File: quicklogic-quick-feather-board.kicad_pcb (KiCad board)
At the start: 2 copper layers, 50.8 x 22.9 mm, 4 parts, among them IC1 EOS-S3, J5 0473460001

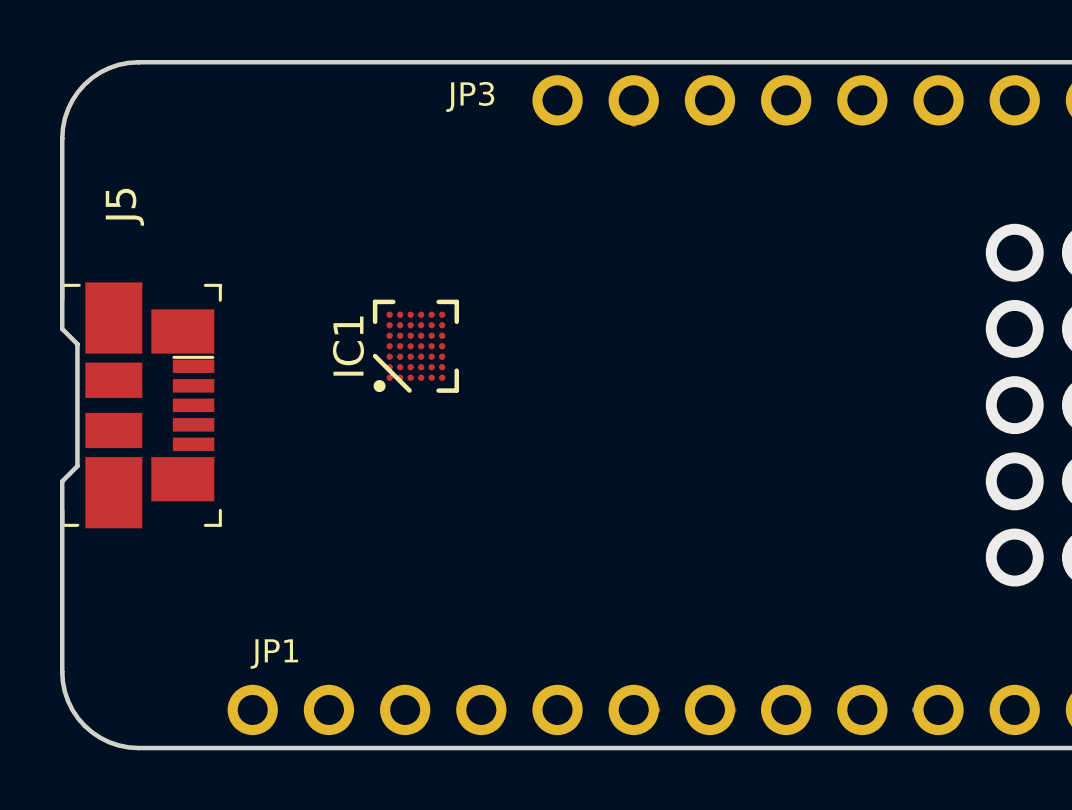
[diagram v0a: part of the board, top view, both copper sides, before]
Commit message: Added power supply circuits
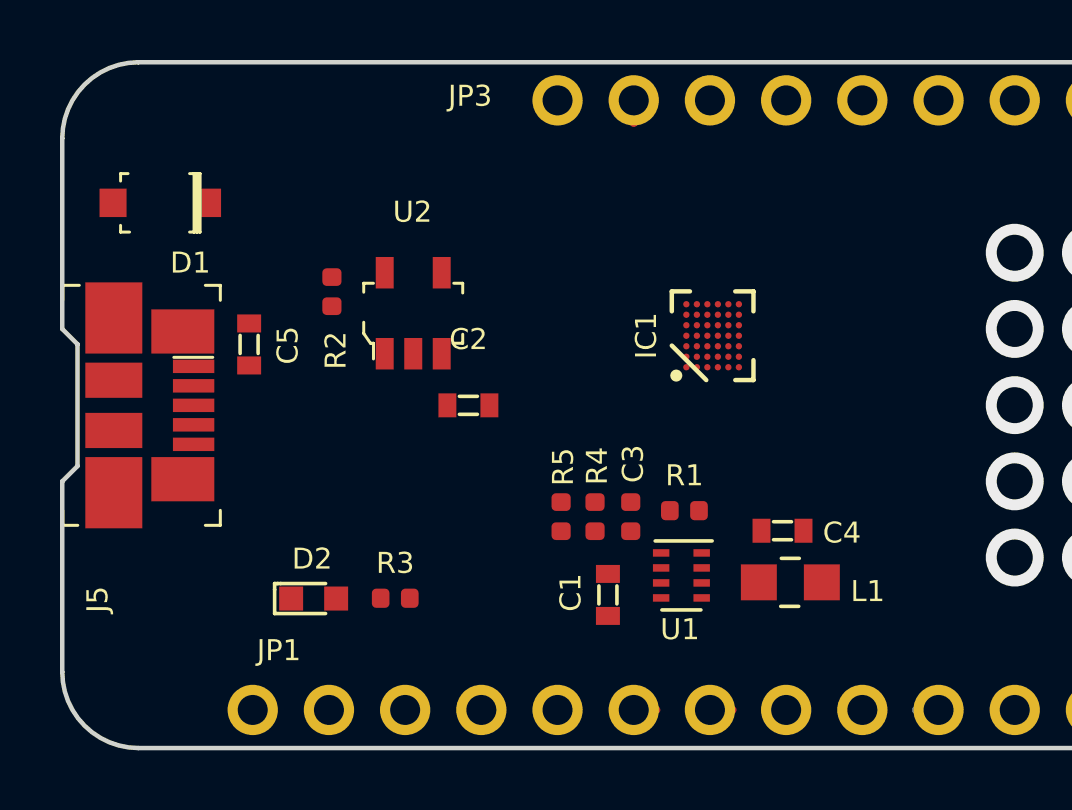
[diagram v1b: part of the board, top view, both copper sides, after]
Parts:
- added C1: C_4u7_0603, antmicro-footprints:0603-cap, F.Cu at (141.3, 111.3)
- added C2: C_10u_0603, antmicro-footprints:0603-cap, F.Cu at (136.6, 105.0)
- added C3: C_100p_0402, antmicro-footprints:0402-cap, F.Cu at (142.1, 108.7)
- added C4: C_22u_0603, antmicro-footprints:0603-cap, F.Cu at (147.1, 109.2)
- added C5: C_10u_0603, antmicro-footprints:0603-cap, F.Cu at (129.3, 103.0)
- added D1: MBR0520LT1G, antmicro-footprints:SOD-123, F.Cu at (126.4, 98.3)
- added D2: LG_L29K-G2J1-24-Z, antmicro-footprints:LED_0603, F.Cu at (131.5, 111.5)
- added L1: DFE201610E-R47M=P2, antmicro-footprints:0805-res, F.Cu at (147.4, 110.9)
- added R1: R_100k_0402, antmicro-footprints:0402-res, F.Cu at (143.8, 108.5)
- added R2: R_5k11_0402, antmicro-footprints:0402-res, F.Cu at (132.1, 101.2)
- added R3: R_1k_0402, antmicro-footprints:0402-res, F.Cu at (134.2, 111.4)
- added R4: R_100k_0402, antmicro-footprints:0402-res, F.Cu at (140.9, 108.7)
- added R5: R_100k_0402, antmicro-footprints:0402-res, F.Cu at (139.7, 108.7)
- added U1: TPS62821DLCR, antmicro-footprints:QFN-8_2x1mm, F.Cu at (143.7, 110.7)
- added U2: MCP73831T-2ACI_OT, antmicro-footprints:SOT-753, F.Cu at (134.8, 101.9)
- moved IC1 9.90 mm to (144.8, 102.7)
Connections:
- J5 pad 1: /5V0_USB -> /VBUS

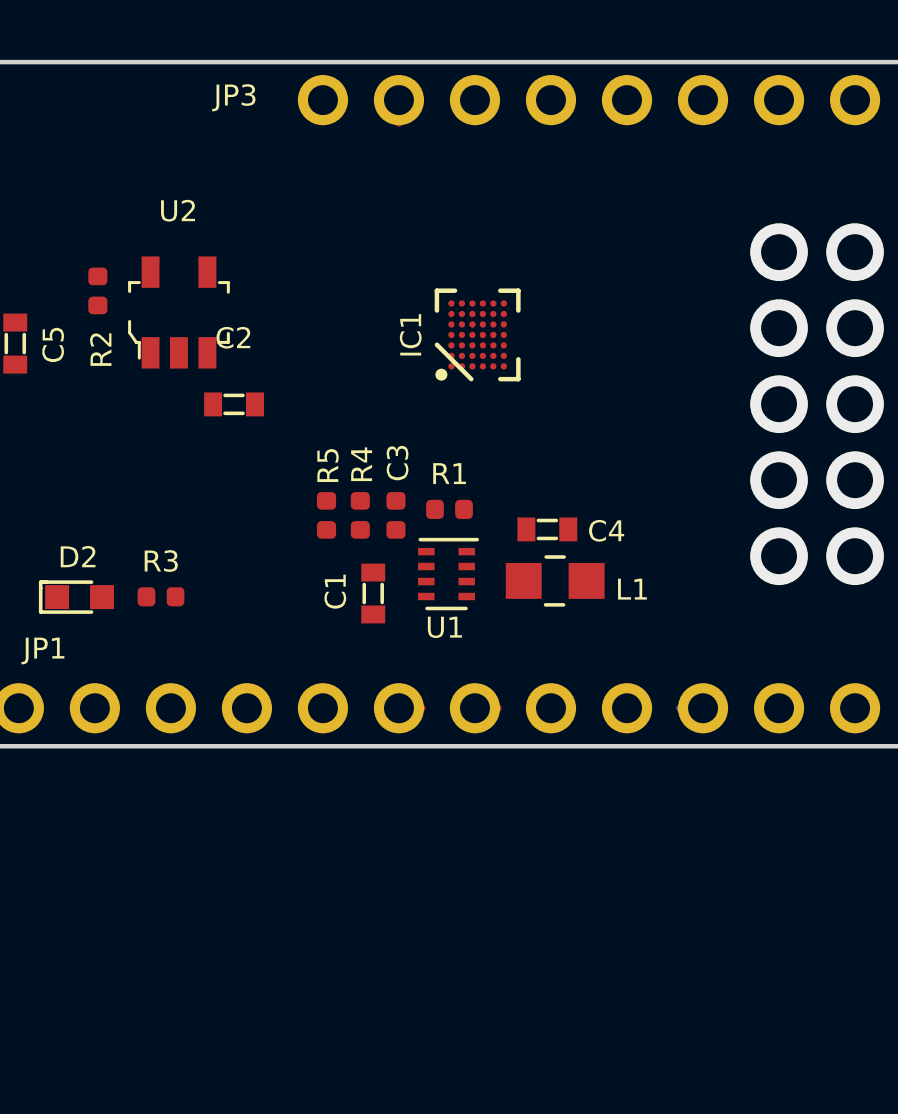
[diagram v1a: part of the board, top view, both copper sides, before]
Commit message: Added flash memory and 32kHz crystal
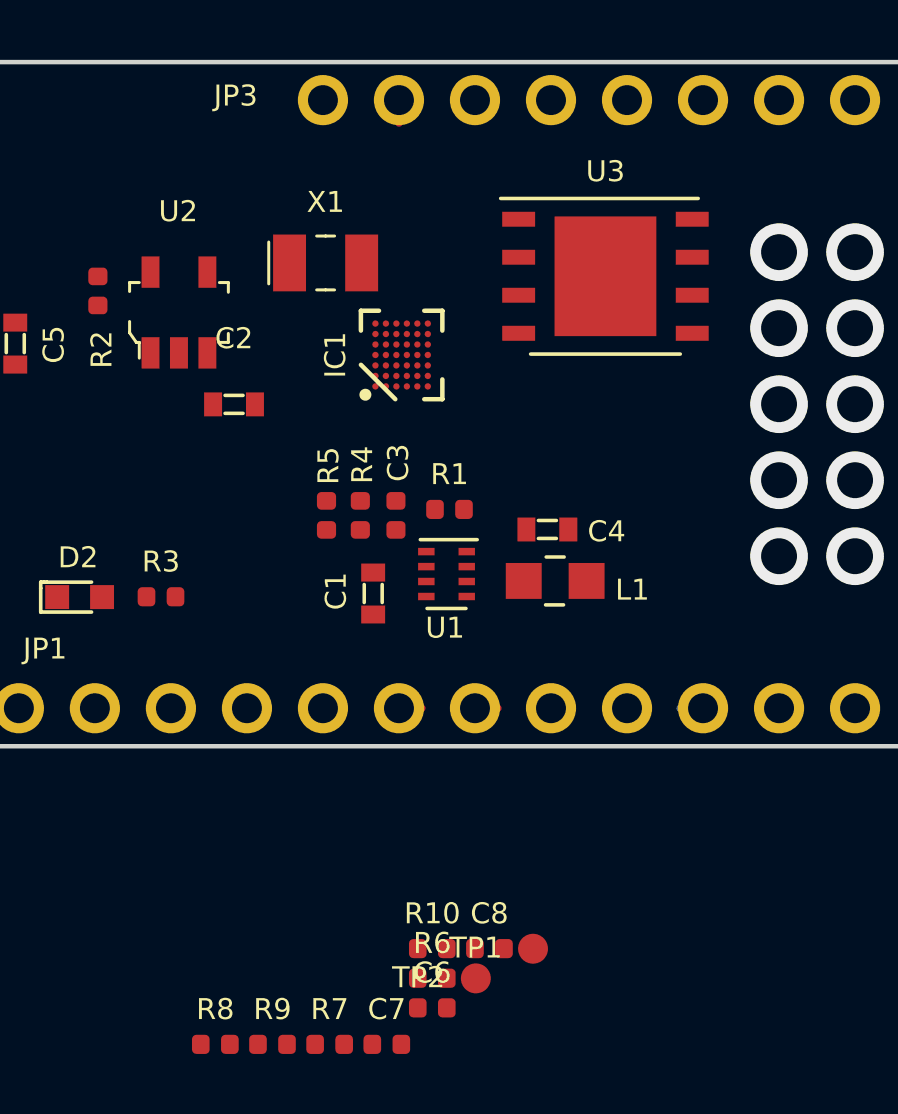
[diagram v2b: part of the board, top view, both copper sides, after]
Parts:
- added C6: C_12p_0402, antmicro-footprints:0402-cap, F.Cu at (143.3, 125.2)
- added C7: C_12p_0402, antmicro-footprints:0402-cap, F.Cu at (141.7, 126.4)
- added C8: C_100n_0402_6V3, antmicro-footprints:0402-cap, F.Cu at (145.2, 123.2)
- added R10: R_10k_0402, antmicro-footprints:0402-res, F.Cu at (143.3, 123.2)
- added R6: R_10k_0402, antmicro-footprints:0402-res, F.Cu at (143.3, 124.2)
- added R7: R_0R_0402, antmicro-footprints:0402-res, F.Cu at (139.8, 126.4)
- added R8: R_10k_0402, antmicro-footprints:0402-res, F.Cu at (136.0, 126.4)
- added R9: R_10k_0402, antmicro-footprints:0402-res, F.Cu at (137.9, 126.4)
- added TP1: TP_SMD1MM, antmicro-footprints:Testpoint_smd_1mm, F.Cu at (146.6, 123.3)
- added TP2: TP_SMD1MM, antmicro-footprints:Testpoint_smd_1mm, F.Cu at (144.7, 124.2)
- added U3: MX25U6435FZNI-10G, antmicro-footprints:DFN-8-1EP_6x5mm_P1.27mm_EP4x3.4mm, F.Cu at (149.1, 100.7)
- added X1: ECS-_327-12_5-34B-TR, antmicro-footprints:SMD-2_3.2x1.5mm, F.Cu at (139.7, 100.3)
- R4: value R_100k_0402 -> R_453k_0402
- moved IC1 2.63 mm to (142.2, 103.4)
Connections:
- IC1 pad B3: Net-(IC1-PadB3) -> /EOS_VDD
- IC1 pad C2: Net-(IC1-PadC2) -> /EOS_VDD
- IC1 pad C3: Net-(IC1-PadC3) -> GND
- IC1 pad C4: Net-(IC1-PadC4) -> GND
- IC1 pad C5: Net-(IC1-PadC5) -> GND
- IC1 pad C6: Net-(IC1-PadC6) -> /EOS_VDD
- IC1 pad D4: Net-(IC1-PadD4) -> GND
- IC1 pad D6: Net-(IC1-PadD6) -> /EOS_VDD
- IC1 pad F1: Net-(IC1-PadF1) -> /RST_N

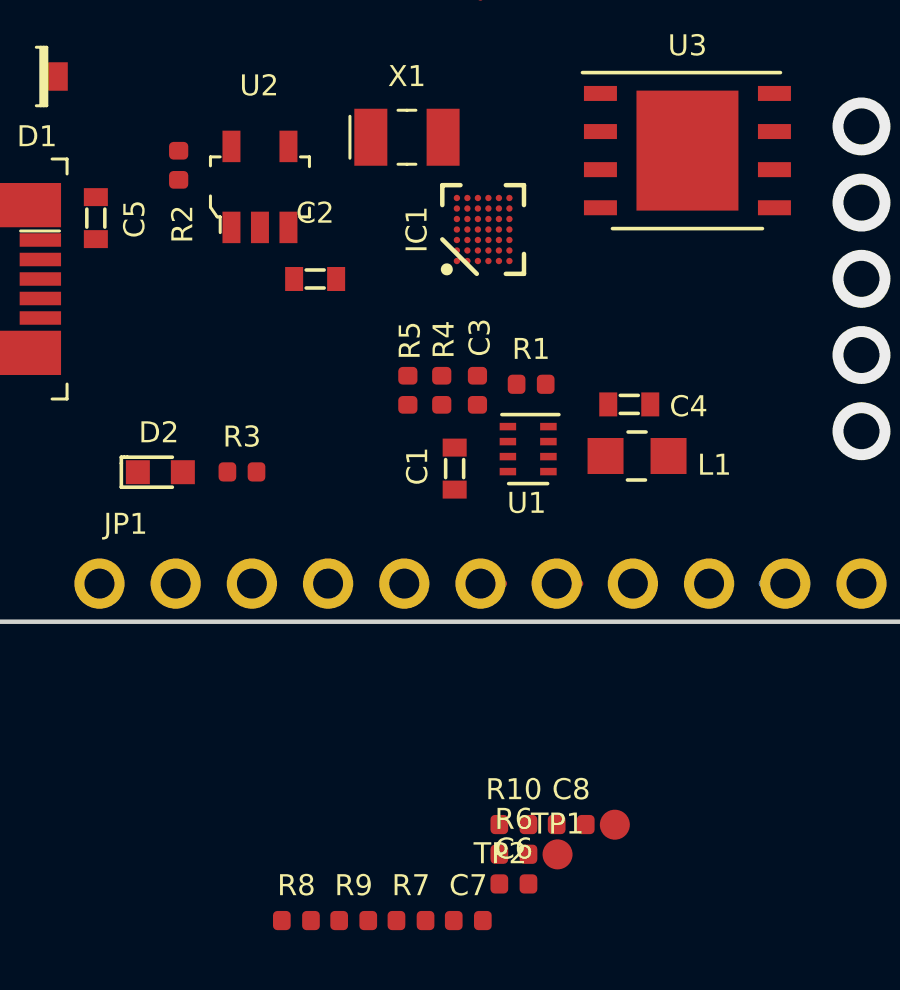
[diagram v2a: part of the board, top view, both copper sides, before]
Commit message: Updated design rules, proposed initial package escape for 42-WLCSP
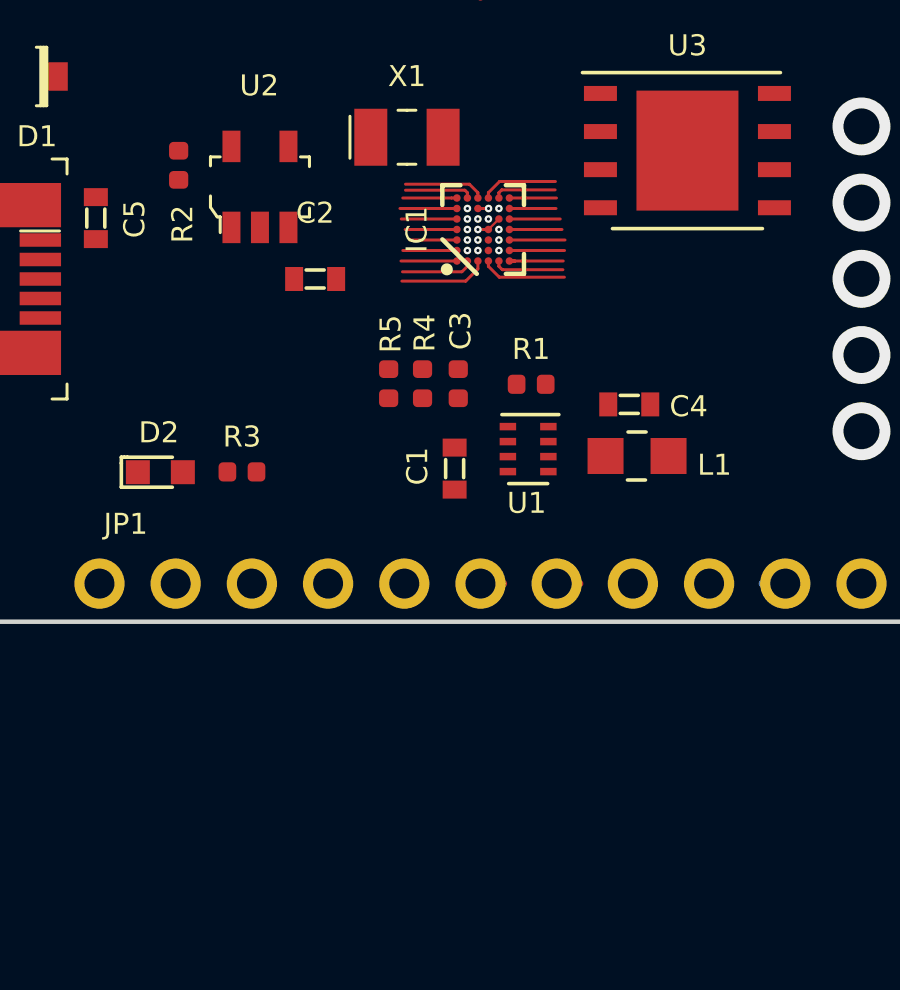
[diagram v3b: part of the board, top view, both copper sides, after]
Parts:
- removed C6, C7: C_12p_0402, antmicro-footprints:0402-cap
- removed C8: C_100n_0402_6V3, antmicro-footprints:0402-cap
- removed R10, R6, R8, R9: R_10k_0402, antmicro-footprints:0402-res
- removed R7: R_0R_0402, antmicro-footprints:0402-res
- removed TP1, TP2: TP_SMD1MM, antmicro-footprints:Testpoint_smd_1mm
- moved C3 0.68 mm to (141.4, 108.5)
- moved R4 0.68 mm to (140.2, 108.5)
- moved R5 0.68 mm to (139.1, 108.5)
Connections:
- IC1 pad E5: Net-(IC1-PadE5) -> GND
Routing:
- net /EOS_VDD: track 0.00 -> 6.03 mm, vias 0 -> 3
- net Net-(IC1-PadC1): track 0.00 -> 2.97 mm
- net Net-(IC1-PadD1): track 0.00 -> 2.86 mm
- net Net-(IC1-PadC7): track 0.00 -> 2.71 mm
- net Net-(IC1-PadD7): track 0.00 -> 2.57 mm
- net Net-(C7-Pad1): track 0.00 -> 2.42 mm
- net Net-(IC1-PadB6): track 0.00 -> 2.38 mm, vias 0 -> 1
- net Net-(IC1-PadB4): track 0.00 -> 2.37 mm, vias 0 -> 1
- net Net-(IC1-PadE1): track 0.00 -> 2.36 mm
- net Net-(IC1-PadB7): track 0.00 -> 2.28 mm
- net Net-(IC1-PadB5): track 0.00 -> 2.25 mm, vias 0 -> 1
- net Net-(IC1-PadB2): track 0.00 -> 2.24 mm, vias 0 -> 1
- net Net-(IC1-PadE3): track 0.00 -> 2.20 mm, vias 0 -> 1
- net Net-(IC1-PadE2): track 0.00 -> 2.20 mm, vias 0 -> 1
- net Net-(IC1-PadE6): track 0.00 -> 2.19 mm, vias 0 -> 1
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- added copper zone on In1.Cu, net GND
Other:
- copper layers 2 -> 4
- net class Default: clearance 0.2 -> 0.0762; trace_width 0.25 -> 0.1; via_dia 0.8 -> 0.25; via_drill 0.4 -> 0.1
- rule trace_clearance: 0.2 -> 0.0762
- rule trace_min: 0.2 -> 0.0762
- rule via_min_drill: 0.3 -> 0.1
- rule via_min_size: 0.4 -> 0.25

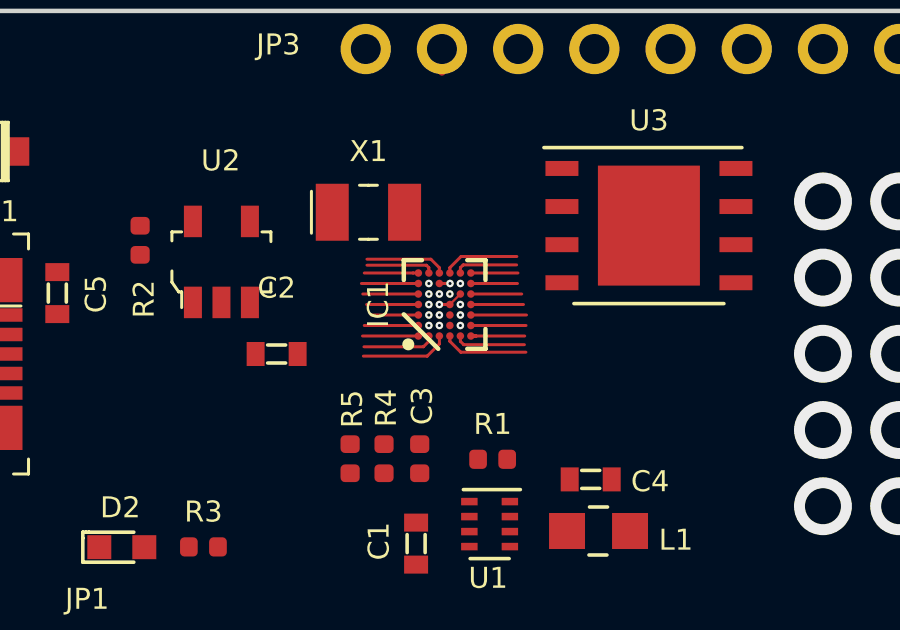
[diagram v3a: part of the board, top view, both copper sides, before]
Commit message: Updated package escape so we are loosing 1 ball of WLCSP
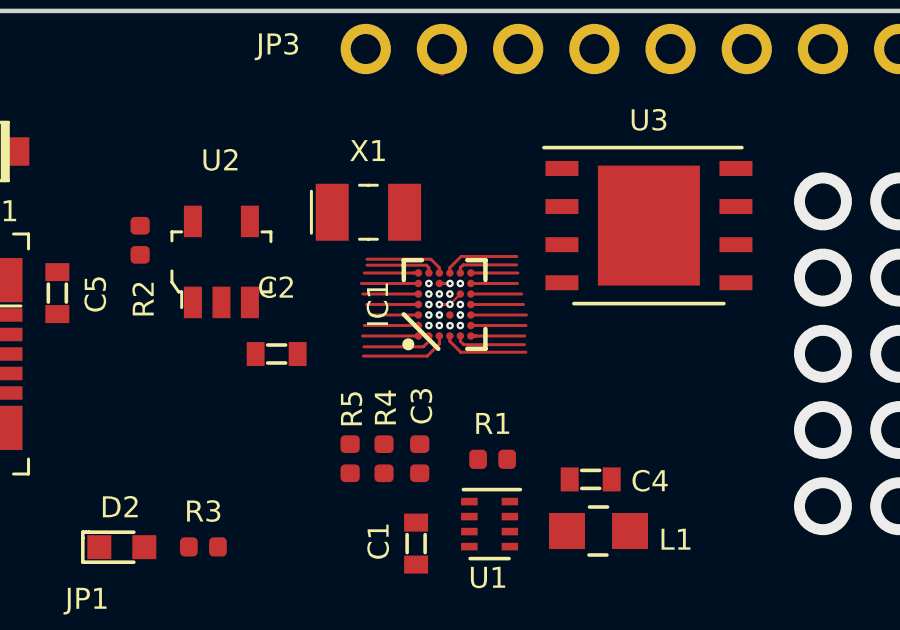
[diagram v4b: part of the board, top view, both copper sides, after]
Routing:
- net Net-(IC1-PadD2): track 0.00 -> 2.26 mm, vias 0 -> 1
- net GND: vias 7 -> 8
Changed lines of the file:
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@@
-(kicad_pcb (version 20171130) (host pcbnew 5.1.4+dfsg1-1~bpo9+1)
+(kicad_pcb (version 20171130) (host pcbnew 5.1.4+dfsg1-1~bpo10+1)
   (general
     (thickness 1.6)
     (drawings 22)
-    (tracks 138)
+    (tracks 143)
     (zones 0)
     (modules 21)
@@
     (0 Top signal)
     (1 In1.Cu signal)
-    (2 In2.Cu signal)
-    (31 Bottom signal)
-    (32 B.Adhes user)
-    (33 F.Adhes user)
-    (34 B.Paste user)
-    (35 F.Paste user)
-    (36 B.SilkS user)
-    (37 F.SilkS user)
-    (38 B.Mask user)
-    (39 F.Mask user)
-    (40 Dwgs.User user)
-    (41 Cmts.User user)
-    (42 Eco1.User user)
-    (43 Eco2.User user)
-    (44 Edge.Cuts user)
-    (45 Margin user)
-    (46 B.CrtYd user)
-    (47 F.CrtYd user)
+    (2 In2.Cu signal hide)
+    (31 Bottom signal hide)
+    (32 B.Adhes user hide)
+    (33 F.Adhes user hide)
+    (34 B.Paste user hide)
+    (35 F.Paste user hide)
+    (36 B.SilkS user hide)
+    (37 F.SilkS user hide)
+    (38 B.Mask user hide)
+    (39 F.Mask user hide)
+    (40 Dwgs.User user hide)
+    (41 Cmts.User user hide)
+    (42 Eco1.User user hide)
+    (43 Eco2.User user hide)
+    (44 Edge.Cuts user hide)
+    (45 Margin user hide)
+    (46 B.CrtYd user hide)
+    (47 F.CrtYd user hide)
     (48 B.Fab user hide)
     (49 F.Fab user hide)
@@
     (arrow2b (pts (xy 118.6561 94.8436) (xy 119.242521 95.970104)))
   )
+  (via micro (at 142.4206 104.0656) (size 0.25) (drill 0.1) (layers Top In1.Cu) (net 75))
+  (via micro (at 142.4178 103.3544) (size 0.25) (drill 0.1) (layers Top In1.Cu) (net 1))
   (via micro (at 142.065 103.71) (size 0.25) (drill 0.1) (layers Top In1.Cu) (net 1))
   (via micro (at 142.065 103.36) (size 0.25) (drill 0.1) (layers Top In1.Cu) (net 1))
@@
   (segment (start 141.715 104.06) (end 141.538224 104.06) (width 0.1) (layer In1.Cu) (net 74))
   (segment (start 141.538224 104.06) (end 139.48 104.06) (width 0.1) (layer In1.Cu) (net 74))
+  (segment (start 142.4206 104.242376) (end 142.673824 104.4956) (width 0.1) (layer In1.Cu) (net 75))
+  (segment (start 142.4206 104.0656) (end 142.4206 104.242376) (width 0.1) (layer In1.Cu) (net 75))
+  (segment (start 142.673824 104.4956) (end 144.399 104.4956) (width 0.1) (layer In1.Cu) (net 75))
   (via micro (at 142.765 104.06) (size 0.25) (drill 0.1) (layers Top In1.Cu) (net 76))
   (segment (start 142.765 104.06) (end 144.96 104.06) (width 0.1) (layer In1.Cu) (net 76))
@@
     (polygon
       (pts
-        (xy 141.9 102.075) (xy 141.9 103.875) (xy 142.25 103.875) (xy 142.25 106.45) (xy 142.6 106.45)
+        (xy 141.9 102.075) (xy 141.9126 103.886) (xy 142.2626 103.886) (xy 142.2682 103.886) (xy 142.5956 103.886)
         (xy 142.6 103.175) (xy 142.25 103.175) (xy 142.25 99.85) (xy 141.9 99.85)
       )
